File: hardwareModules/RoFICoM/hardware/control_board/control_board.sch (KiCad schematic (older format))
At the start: 29 parts, among them J1 Skirt Cable, J2 M+, J3 M-, J4 SWD, J5 DBG_UART, J6 SYS_CON, J7 SLIDER, J8 DBG, J9 SYS_CON_2, U1 STM32G071GBU6, U2 DRV8837C, U3 BU52272NUZ, U4 NCP718ASN330T1G, U5 BU52272NUZ

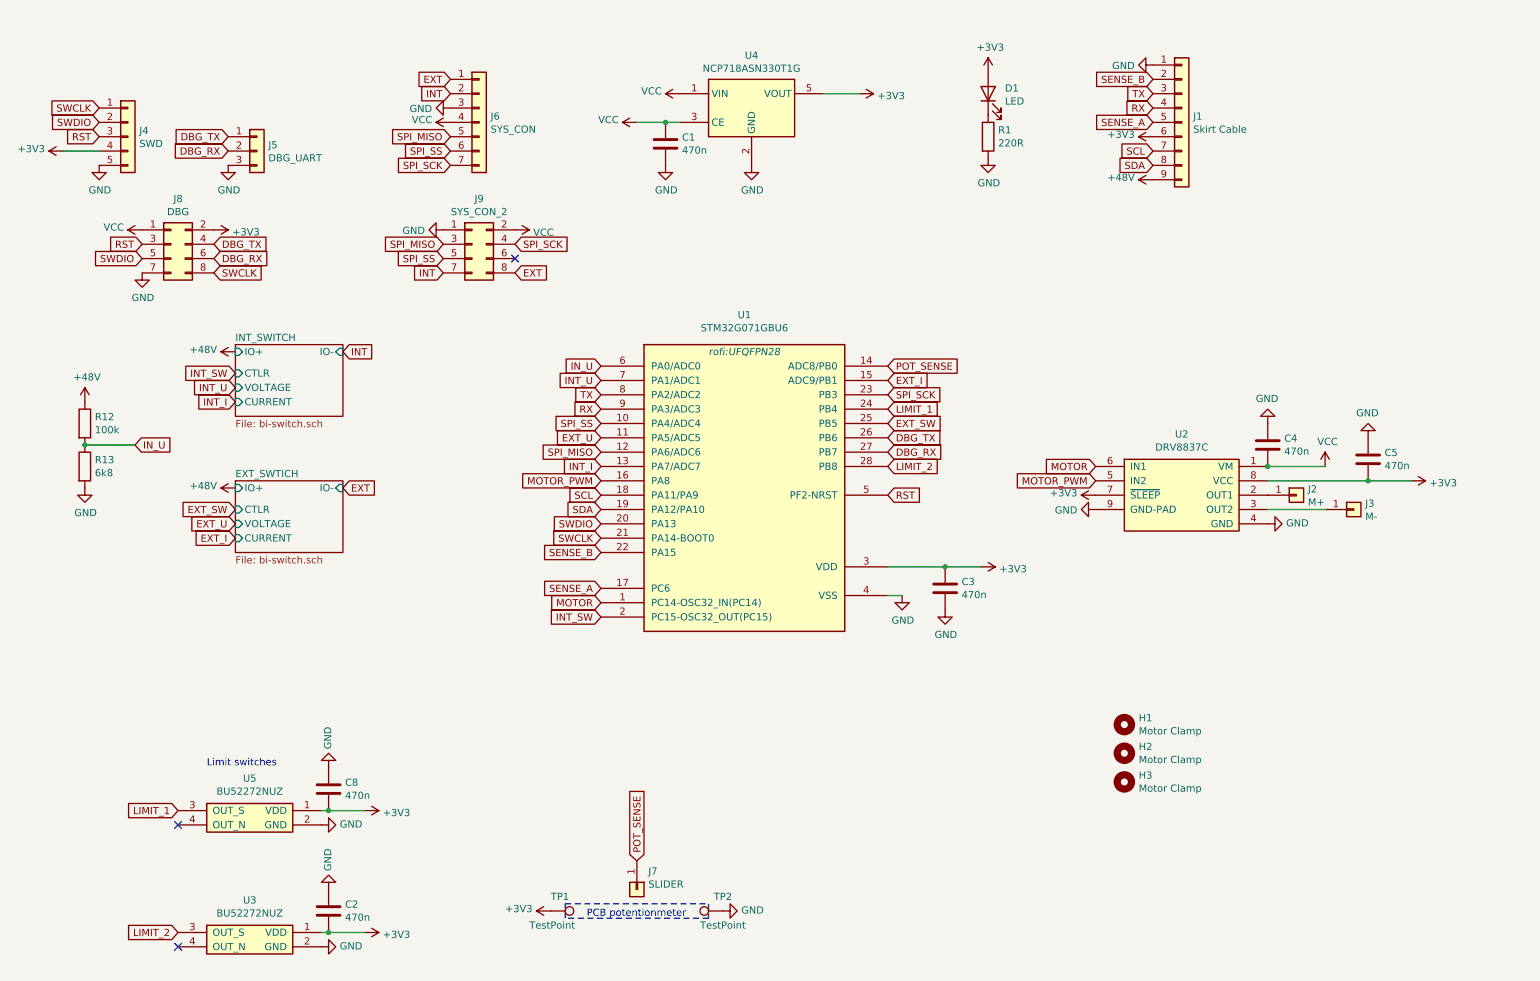
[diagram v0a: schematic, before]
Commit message: universalModule: Prepare electronics v0.2
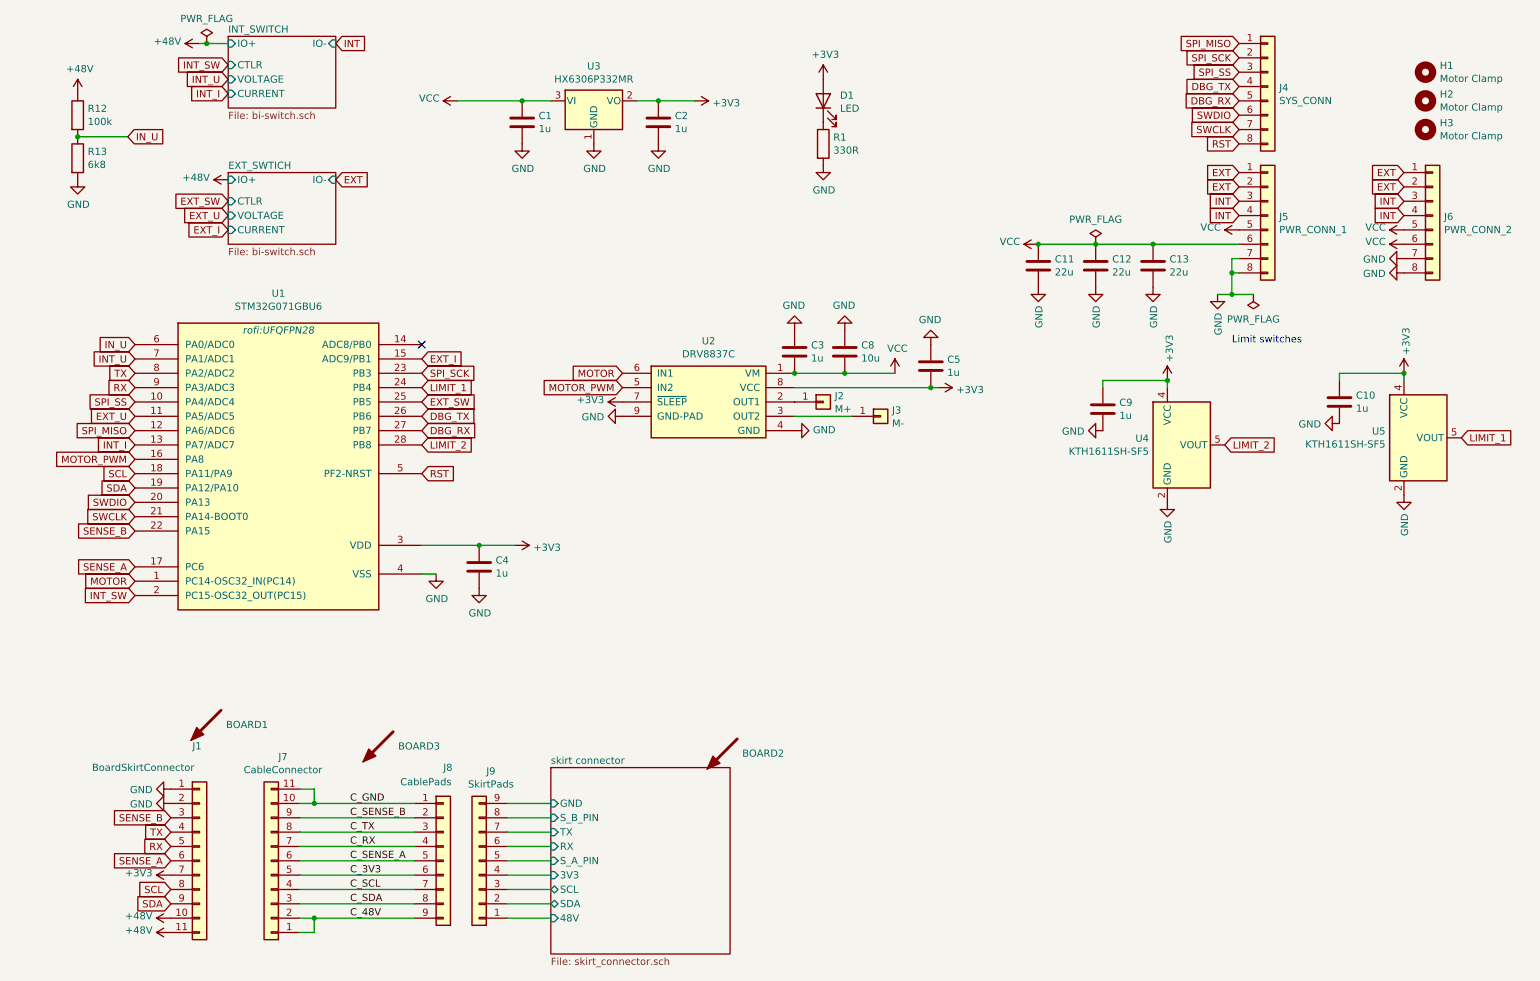
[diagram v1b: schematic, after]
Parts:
- removed J1: Skirt Cable, rofi:flat_cable_9, symbol Connector_Generic:Conn_01x09
- removed J4: SWD, Connector_PinHeader_2.54mm:PinHeader_1x05_P2.54mm_Vertical, symbol Connector_Generic:Conn_01x05
- removed J5: DBG_UART, Connector_PinSocket_2.54mm:PinSocket_1x03_P2.54mm_Vertical, symbol Connector_Generic:Conn_01x03
- removed J6: SYS_CON, rofi:pogo_row_4_3, symbol Connector_Generic:Conn_01x07
- removed J7: SLIDER, Connector_PinHeader_1.27mm:PinHeader_1x01_P1.27mm_Vertical, symbol Connector_Generic:Conn_01x01
- removed J8: DBG, rofi:molex-505006-0812, symbol Connector_Generic:Conn_02x04_Odd_Even
- removed J9: SYS_CON_2, rofi:molex-505006-0812, symbol Connector_Generic:Conn_02x04_Odd_Even
- removed TP1, TP2: TestPoint, TestPoint:TestPoint_Pad_D1.5mm, symbol Connector:TestPoint
- removed U3, U5: BU52272NUZ, rofi:VSON04Z1114A, symbol rofi:BU52272NUZ
- removed U4: NCP718ASN330T1G, Package_TO_SOT_SMD:SOT-23-5, symbol Regulator_Linear:XC6220B331MR
- added BOARD1, BOARD2, BOARD3: BOARD, kikit:Board, symbol Graphic:SYM_Arrow45_Large
- added C10, C9: 1u, Capacitor_SMD:C_0402_1005Metric, symbol Device:C
- added C11, C12, C13: 22u, Capacitor_SMD:C_0805_2012Metric, symbol Device:C
- added J1: BoardSkirtConnector, rofi:FC38-11N1-AHK, symbol Connector_Generic:Conn_01x11
- added J4: SYS_CONN, rofi:SOLO-9258-mating, symbol Connector_Generic:Conn_01x08
- added J5: PWR_CONN_1, rofi:SOLO-9258-mating, symbol Connector_Generic:Conn_01x08
- added J6: PWR_CONN_2, rofi:SOLO-9258-mating, symbol Connector_Generic:Conn_01x08
- added J7: CableConnector, rofi:FPC_PADS_11, symbol Connector_Generic:Conn_01x11
- added J8: CablePads, rofi:RoFICoM_CableFPCPads, symbol Connector_Generic:Conn_01x09
- added J9: SkirtPads, rofi:RoFICoM_CablePads, symbol Connector_Generic:Conn_01x09
- added U3: HX6306P332MR, Package_TO_SOT_SMD:SOT-23, symbol Regulator_Linear:MCP1700-2502E_SOT23
- added U4, U5: KTH1611SH-SF5, Package_TO_SOT_SMD:SOT-553, symbol rofi:KTH1611SH-SF5
- C1, C2, C3, C4, C5: value 470n -> 1u; LCSC (none) -> C52923; manf# CC0402ZRY5V6BB474 -> (none)
- C8: value 470n -> 10u; footprint Capacitor_SMD:C_0402_1005Metric -> Capacitor_SMD:C_0603_1608Metric; LCSC (none) -> C19702; manf# CC0402ZRY5V6BB474 -> (none)
- D1: JLCPCB_CORRECTION (none) -> 0;0;180; LCSC (none) -> C72038; manf# 150060YS75000 -> (none)
- H1, H2, H3: JLCPCB_IGNORE (none) -> YES
- J2, J3: footprint Connector_PinSocket_2.54mm:PinSocket_1x01_P2.54mm_Vertical -> TestPoint:TestPoint_Pad_D2.5mm
- R1: value 220R -> 330R; LCSC (none) -> C25104; manf# RC0402JR-13220RL -> (none)
- R12: LCSC (none) -> C25741; manf# RC0402JR-13100KL -> (none)
- R13: LCSC (none) -> C25917; manf# RC0402FR-076K8L -> (none)
- U1: LCSC (none) -> C529347
- U2: LCSC (none) -> C191000
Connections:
- net +3V3: now also C2.1, C4.1, C10.1, C9.1, J1.7 (Pin_7), U3.2 (VO), U4.4 (VCC), U5.4 (VCC); no longer C2.2, C3.1, C8.2
- net +48V: now also J1.10 (Pin_10), J1.11 (Pin_11)
- net DBG_RX: now also J4.5 (Pin_5)
- net DBG_TX: now also J4.4 (Pin_4)
- net EXT: now also J5.1 (Pin_1), J5.2 (Pin_2), J6.1 (Pin_1), J6.2 (Pin_2)
- net GND: now also C2.2, C3.1, C4.2, C10.2, C11.2, C12.2, C13.2, C9.2, J1.1 (Pin_1), J1.2 (Pin_2), J5.7 (Pin_7), J5.8 (Pin_8), J6.7 (Pin_7), J6.8 (Pin_8), U3.1 (GND), U4.2 (GND), U5.2 (GND); no longer C2.1, C3.2, C4.1
- net INT: now also J5.3 (Pin_3), J5.4 (Pin_4), J6.3 (Pin_3), J6.4 (Pin_4)
- net LIMIT_1: now also U5.5 (VOUT)
- net LIMIT_2: now also U4.5 (VOUT)
- net RST: now also J4.8 (Pin_8)
- net RX: now also J1.5 (Pin_5)
- net SCL: now also J1.8 (Pin_8)
- net SDA: now also J1.9 (Pin_9)
- net SENSE_A: now also J1.6 (Pin_6)
- net SENSE_B: now also J1.3 (Pin_3)
- net SPI_MISO: now also J4.1 (Pin_1)
- net SPI_SCK: now also J4.2 (Pin_2)
- net SPI_SS: now also J4.3 (Pin_3)
- net SWCLK: now also J4.7 (Pin_7)
- net SWDIO: now also J4.6 (Pin_6)
- net TX: now also J1.4 (Pin_4)
- net VCC: now also C3.2, C8.2, C11.1, C12.1, C13.1, J5.5 (Pin_5), J5.6 (Pin_6), J6.5 (Pin_5), J6.6 (Pin_6), U3.3 (VI); no longer C4.2
- net POT_SENSE: no longer names the net of U1.14 (ADC8/PB0)
- new net C_3V3: J7.5 (Pin_5), J8.6 (Pin_6)
- new net C_48V: J7.1 (Pin_1), J7.2 (Pin_2), J8.9 (Pin_9)
- new net C_GND: J7.10 (Pin_10), J7.11 (Pin_11), J8.1 (Pin_1)
- new net C_RX: J7.7 (Pin_7), J8.4 (Pin_4)
- new net C_SCL: J7.4 (Pin_4), J8.7 (Pin_7)
- new net C_SDA: J7.3 (Pin_3), J8.8 (Pin_8)
- new net C_SENSE_A: J7.6 (Pin_6), J8.5 (Pin_5)
- new net C_SENSE_B: J7.9 (Pin_9), J8.2 (Pin_2)
- new net C_TX: J7.8 (Pin_8), J8.3 (Pin_3)
- new net skirt connector/3V3: J9.4 (Pin_4)
- new net skirt connector/48V: J9.1 (Pin_1)
- new net skirt connector/GND: J9.9 (Pin_9)
- new net skirt connector/RX: J9.6 (Pin_6)
- new net skirt connector/SCL: J9.3 (Pin_3)
- new net skirt connector/SDA: J9.2 (Pin_2)
- new net skirt connector/S_A_PIN: J9.5 (Pin_5)
- new net skirt connector/S_B_PIN: J9.8 (Pin_8)
- new net skirt connector/TX: J9.7 (Pin_7)
- no-connect marks 3 -> 1
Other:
- note removed: "PCB potentionmeter"
- moved on the sheet: C4, C5, D1, H1, H2, H3, J2, J3, R1, R12, R13, U1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

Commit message: universalModule: Add final pre-production tweaks
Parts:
- D1: JLCPCB_CORRECTION 0;0;180 -> (none)
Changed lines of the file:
@@
 F 3 "~" H 6250 1350 50  0001 C CNN
 F 4 "C72038" H -1150 50  50  0001 C CNN "LCSC"
-F 5 "0;0;180" V 6250 1350 50  0001 C CNN "JLCPCB_CORRECTION"
 	1    6250 1350
 	0    -1   -1   0
